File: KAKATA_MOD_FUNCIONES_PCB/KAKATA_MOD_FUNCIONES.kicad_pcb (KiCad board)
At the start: 4 copper layers, 80.3 x 64.3 mm, 61 parts, among them J1 DB128L-5.08-2P-BK-S, J2 Screw_Terminal_01x02, J3 Screw_Terminal_01x02, J4 Screw_Terminal_01x02, J5 DB125-2.54-10P-GN, J6 DB125-2.54-4P-GN, Q1 MMUN2215L, Q2 MMUN2215L, Q3 MMUN2215L, U1 ESP32-S3-WROOM-1(N16R8), U2 PS-TO220, U3 PS-TO220, U4 TYPE-C 16PLT-H10.0

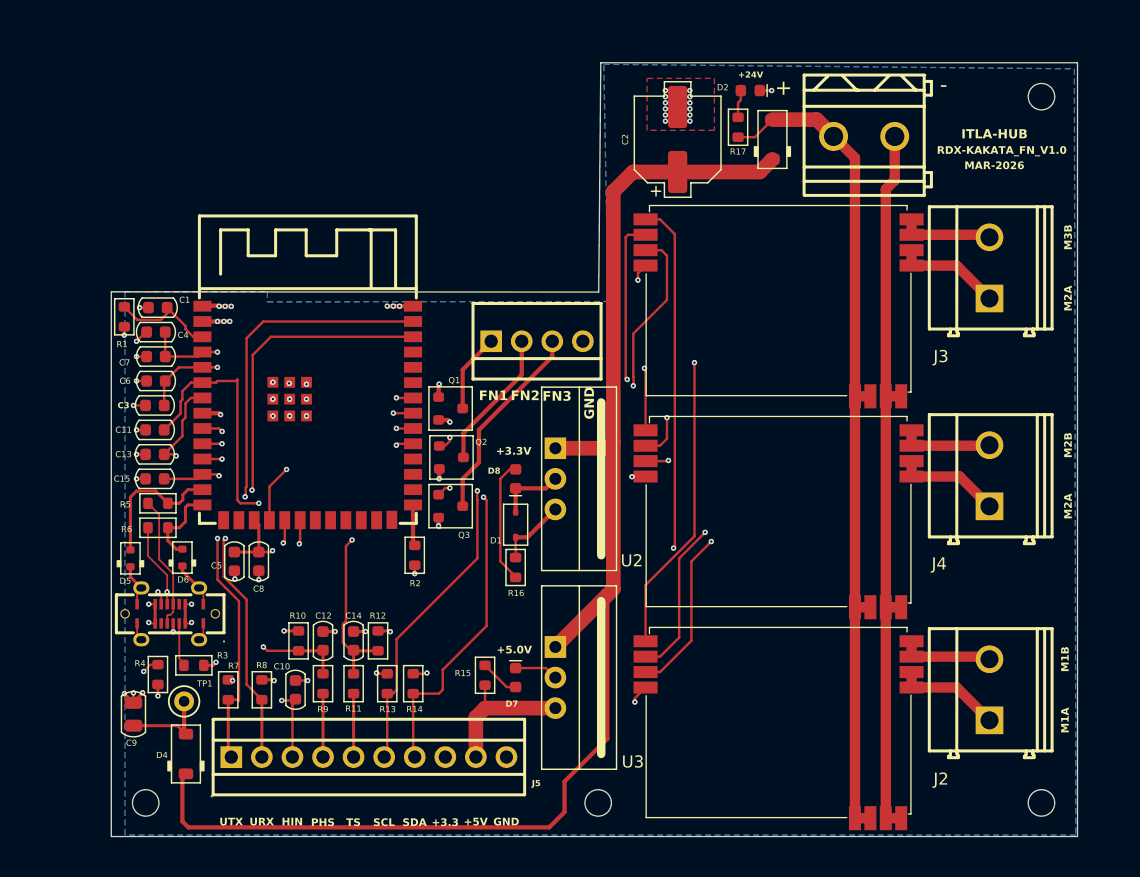
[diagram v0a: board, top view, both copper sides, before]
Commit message: Btn's BOOT y RST agregados. Encendido secuencial implementado
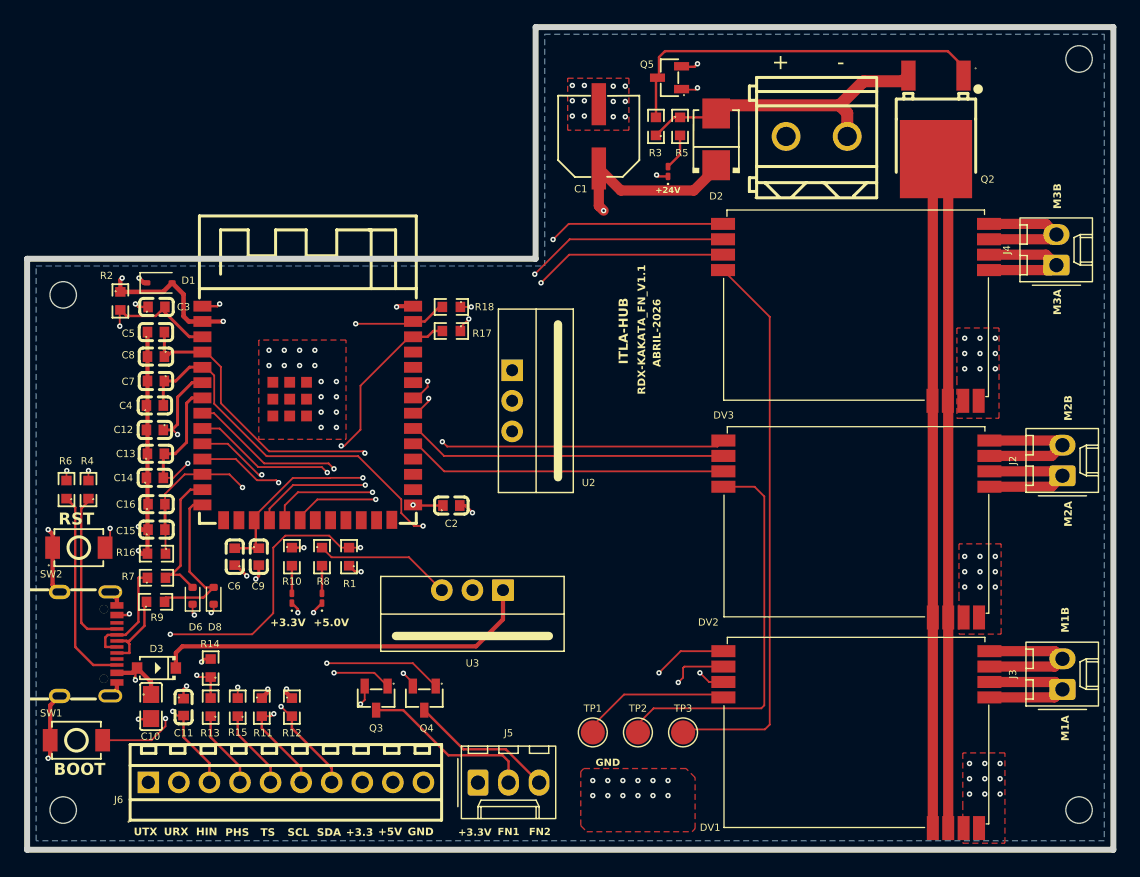
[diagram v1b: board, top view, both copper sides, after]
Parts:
- removed the C1 at (83.1, 63.6)
- removed the D4 at (85.5, 100.6)
- removed Q1: MMUN2215L, PCM_Package_TO_SOT_SMD_AKL:SOT-23
- removed the R15 at (110.3, 94.1)
- removed the R16 at (112.9, 85.2)
- removed U4: TYPE-C 16PLT-H10.0, EasyEDA:TYPE-C-SMD_USB4120-03-C
- added C2: 0.1uF, EasyEDA:C0603, F.Cu at (107.5, 80.0)
- added C3: 1uF, EasyEDA:C0603, F.Cu at (83.0, 63.5)
- added D3: B0540W, EasyEDA:SOD-123_L2.7-W1.6-LS3.7-FD, F.Cu at (83.0, 93.5)
- added Q4: MMUN2215LT1G, EasyEDA:SOT-23-3_L2.9-W1.3-P1.90-LS2.4-BR, F.Cu at (105.3, 96.0)
- added Q5: MMUN2215LT1G, EasyEDA:SOT-23-3_L2.9-W1.3-P1.90-LS2.4-BR, F.Cu at (125.7, 44.5)
- added R10: 220, EasyEDA:R0603, F.Cu at (94.3, 84.3)
- added R3: 10k, EasyEDA:R0603, F.Cu at (124.5, 48.5)
- added R9: 33R, EasyEDA:R0603, F.Cu at (83.0, 88.0)
- added SW1: TS-1088-AR02016, EasyEDA:SW-SMD_L3.9-W3.0-P4.45, F.Cu at (76.4, 99.5)
- added SW2: TS-1088-AR02016, EasyEDA:SW-SMD_L3.9-W3.0-P4.45, F.Cu at (76.6, 83.5)
- added TP2: TestPoint, TestPoint:TestPoint_Pad_D2.0mm, F.Cu at (123.0, 98.9)
- added TP3: TestPoint, TestPoint:TestPoint_Pad_D2.0mm, F.Cu at (126.8, 98.9)
- added USB1: TYPE-C 16PIN 2MD, EasyEDA:USB-C-SMD_TYPE-C-6PIN-2MD-073, F.Cu at (77.4, 91.5)
- C1: renamed from C2; footprint Capacitor_SMD_AKL:CP_Elec_6.3x7.7 -> EasyEDA:CAP-SMD_BD6.3-L6.6-W6.6-LS7.2-FD
- C10: renamed from C9; footprint PCM_Capacitor_SMD_AKL:C_0805_2012Metric -> EasyEDA:C0805
- C11: renamed from C10; footprint PCM_Capacitor_SMD_AKL:C_0603_1608Metric -> EasyEDA:C0603
- C12: renamed from C11; footprint PCM_Capacitor_SMD_AKL:C_0603_1608Metric -> EasyEDA:C0603
- C13: renamed from C12; footprint PCM_Capacitor_SMD_AKL:C_0603_1608Metric -> EasyEDA:C0603
- C14: renamed from C13; footprint PCM_Capacitor_SMD_AKL:C_0603_1608Metric -> EasyEDA:C0603
- C15: renamed from C14; footprint PCM_Capacitor_SMD_AKL:C_0603_1608Metric -> EasyEDA:C0603
- C16: renamed from C15; footprint PCM_Capacitor_SMD_AKL:C_0603_1608Metric -> EasyEDA:C0603
- C4: renamed from C3; footprint PCM_Capacitor_SMD_AKL:C_0603_1608Metric -> EasyEDA:C0603
- C5: renamed from C4; footprint PCM_Capacitor_SMD_AKL:C_0603_1608Metric -> EasyEDA:C0603
- C6: renamed from C5; footprint PCM_Capacitor_SMD_AKL:C_0603_1608Metric -> EasyEDA:C0603
- C7: renamed from C6; footprint PCM_Capacitor_SMD_AKL:C_0603_1608Metric -> EasyEDA:C0603
- C8: renamed from C7; footprint PCM_Capacitor_SMD_AKL:C_0603_1608Metric -> EasyEDA:C0603
- C9: renamed from C8; footprint PCM_Capacitor_SMD_AKL:C_0603_1608Metric -> EasyEDA:C0603
- D1: footprint Diode_SMD_AKL:D_SOD-323_TVS -> Diode_SMD:D_SOD-323
- D2: value B0540LW -> SS24-SMB; footprint Diode_SMD_AKL:D_SOD-123 -> EasyEDA:SMB_L4.3-W3.6-LS5.3-RD
- D4: renamed from D5; value ESD5B5.0S -> Red; footprint PCM_Diode_SMD_AKL:D_SOD-523 -> LED_SMD:LED_0201_0603Metric_Pad0.64x0.40mm_HandSolder
- D5: renamed from D6; value ESD5B5.0S -> Red; footprint PCM_Diode_SMD_AKL:D_SOD-523 -> LED_SMD:LED_0201_0603Metric_Pad0.64x0.40mm_HandSolder
- D6: renamed from D9; value Red -> ESD5B5.0S; footprint SparkFun-LED:LED_0603_1608Metric_Red -> Diode_SMD:D_SOD-523
- D7: footprint SparkFun-LED:LED_0603_1608Metric_Red -> LED_SMD:LED_0201_0603Metric_Pad0.64x0.40mm_HandSolder
- D8: value Red -> ESD5B5.0S; footprint SparkFun-LED:LED_0603_1608Metric_Red -> Diode_SMD:D_SOD-523
- DV1, DV2, DV3: footprint ItlaModules:PHE-3A -> ITLA_Modules:PHE-3A
- J2, J3, J4: value Screw_Terminal_01x02 -> Conn_01x02_Socket; footprint EasyEDA:CONN-TH_2P-P5.08_DIBO_DB128V-5.08 -> Connector_Molex:Molex_KK-254_AE-6410-02A_1x02_P2.54mm_Vertical
- J5: value DB125-2.54-10P-GN -> Conn_01x03_Socket; footprint EasyEDA:CONN-TH_DB125-2.54-10P-GN -> Connector_Molex:Molex_KK-254_AE-6410-03A_1x03_P2.54mm_Vertical
- J6: value DB125-2.54-4P-GN -> DB125-2.54-10P-GN; footprint EasyEDA:CONN-TH_DB125-2.54-4P-GN -> EasyEDA:CONN-TH_DB125-2.54-10P-GN
- Q2: value MMUN2215L -> AOD4185_C400894; footprint PCM_Package_TO_SOT_SMD_AKL:SOT-23 -> EasyEDA:TO-252-3_L6.6-W6.1-P4.57-LS9.9-BR-CW
- Q3: value MMUN2215L -> MMUN2215LT1G; footprint PCM_Package_TO_SOT_SMD_AKL:SOT-23 -> EasyEDA:SOT-23-3_L2.9-W1.3-P1.90-LS2.4-BR
- R1: footprint Resistor_SMD_AKL:R_0603_1608Metric -> EasyEDA:R0603
- R11: renamed from R9; value 2.5K -> 4.7K; footprint PCM_Resistor_SMD_AKL:R_0603_1608Metric -> EasyEDA:R0603
- R12: renamed from R10; value 5K -> 4.7K; footprint PCM_Resistor_SMD_AKL:R_0603_1608Metric -> EasyEDA:R0603
- R13: renamed from R11; value 2.5K -> 5.1K; footprint PCM_Resistor_SMD_AKL:R_0603_1608Metric -> EasyEDA:R0603
- R14: renamed from R12; value 5K -> 5.1K; footprint PCM_Resistor_SMD_AKL:R_0603_1608Metric -> EasyEDA:R0603
- R15: renamed from R7; value 4.5K -> 5.1K; footprint PCM_Resistor_SMD_AKL:R_0603_1608Metric -> EasyEDA:R0603
- R16: renamed from R13; value 2.2K -> 5.1K; footprint PCM_Resistor_SMD_AKL:R_0603_1608Metric -> EasyEDA:R0603
- R17: renamed from R8; value 4.5K -> 4.7K; footprint PCM_Resistor_SMD_AKL:R_0603_1608Metric -> EasyEDA:R0603
- R18: renamed from R14; value 2.2K -> 4.7K; footprint PCM_Resistor_SMD_AKL:R_0603_1608Metric -> EasyEDA:R0603
- R2: footprint PCM_Resistor_SMD_AKL:R_0603_1608Metric -> EasyEDA:R0603
- R4: renamed from R3; footprint PCM_Resistor_SMD_AKL:R_0603_1608Metric -> EasyEDA:R0603
- R5: renamed from R4; value 5.1K -> 4.7K; footprint PCM_Resistor_SMD_AKL:R_0603_1608Metric -> EasyEDA:R0603
- R6: renamed from R5; value 33R -> 5.1K; footprint PCM_Resistor_SMD_AKL:R_0603_1608Metric -> EasyEDA:R0603
- R7: renamed from R6; footprint PCM_Resistor_SMD_AKL:R_0603_1608Metric -> EasyEDA:R0603
- R8: renamed from R17; value 4.7K -> 560; footprint Resistor_SMD_AKL:R_0603_1608Metric -> EasyEDA:R0603
- TP1: value TestPoint_Hole1 -> TestPoint; footprint 4ms_TestPoint:TestPoint_WireHole -> TestPoint:TestPoint_Pad_D2.0mm
- moved R5 62.9 mm to (126.5, 48.5)
- moved D6 62.5 mm to (86.0, 87.5), turned to 90 degrees
- moved H4 61.3 mm to (75.3, 62.5)
- moved D4 55.0 mm to (125.5, 52.3)
- moved R8 49.7 mm to (96.8, 84.3), turned to -90 degrees
- moved Q2 49.2 mm to (147.8, 47.8), turned to 90 degrees
- moved J6 42.2 mm to (93.8, 103.0)
- moved D1 35.8 mm to (83.3, 61.5), turned to 0 degrees
- moved J3 35.5 mm to (158.3, 95.3)
- moved TP1 34.1 mm to (119.3, 98.9)
- moved R17 33.7 mm to (107.5, 65.5), turned to 180 degrees
- moved R2 32.3 mm to (80.0, 63.0), turned to -90 degrees
- moved R18 31.5 mm to (107.5, 63.5), turned to 180 degrees
- moved R1 27.3 mm to (99.0, 84.3)
- moved D8 26.9 mm to (87.8, 87.5)
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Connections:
- D4 pad 2: /USB_D- -> Net-(D4-A)
- D5 pad 2: /USB_D+ -> Net-(D5-A)
- D6 pad 2: Net-(D9-A) -> /USB_D-
- D8 pad 2: Net-(D8-A) -> /USB_D+
- DV1 pad 12: +24V -> V_DRIVER
- DV1 pad 4: +3.3V -> Net-(DV1-Vref)
- DV1 pad 8: +24V -> V_DRIVER
- DV2 pad 12: +24V -> V_DRIVER
- DV2 pad 4: +3.3V -> Net-(DV2-Vref)
- DV2 pad 8: +24V -> V_DRIVER
- DV3 pad 12: +24V -> V_DRIVER
- DV3 pad 4: +3.3V -> Net-(DV3-Vref)
- DV3 pad 8: +24V -> V_DRIVER
- J2 pad 1: /MOTOR1_A -> /MOTOR2_A
- J2 pad 2: /MOTOR1_B -> /MOTOR2_B
- J3 pad 1: /MOTOR3_A -> /MOTOR1_A
- J3 pad 2: /MOTOR3_B -> /MOTOR1_B
- J4 pad 1: /MOTOR2_A -> /MOTOR3_A
- J4 pad 2: /MOTOR2_B -> /MOTOR3_B
- J5 pad 1: /UART_TXD_CO2 -> +3.3V
- J5 pad 2: /UART_RXD_CO2 -> Net-(J5-Pin_2)
- J5 pad 3: /H_IN -> Net-(J5-Pin_3)
- J6 pad 1: /FN1 -> /UART_TXD_CO2
- J6 pad 2: /FN2 -> /UART_RXD_CO2
- J6 pad 3: /FN3 -> /H_IN
- J6 pad 4: GND -> /CON_PH_SENSE
- Q2 pad 1: /ACT_2 -> Net-(Q2-G)
- Q2 pad 2: GND -> V_DRIVER
- Q2 pad 3: /FN2 -> +24V
- Q3 pad 1: /ACT_3 -> /ACT_1
- Q3 pad 3: /FN3 -> Net-(J5-Pin_2)
- R1 pad 2: /EN -> /BOOT
- R11 pad 1: /CON_PH_SENSE -> +3.3V
- R11 pad 2: /PH_SENSE -> /I2C_SCL
- R12 pad 1: /PH_SENSE -> +3.3V
- R12 pad 2: GND -> /I2C_SDA
- R13 pad 1: /CON_T_SENSE -> /CON_PH_SENSE
- R13 pad 2: /T_SENSE -> /PH_SENSE
- R14 pad 1: /T_SENSE -> /PH_SENSE
- R15 pad 1: +3.3V -> /CON_T_SENSE
- R15 pad 2: /UART_TXD_CO2 -> /T_SENSE
- R16 pad 1: +3.3V -> /T_SENSE
- R16 pad 2: /I2C_SCL -> GND
- R17 pad 2: /UART_RXD_CO2 -> /UART_TXD_CO2
- R18 pad 2: /I2C_SDA -> /UART_RXD_CO2
- R2 pad 2: /BOOT -> /CHIP_PU
- R5 pad 1: Net-(U4-CC2) -> +24V
- R5 pad 2: GND -> Net-(D4-A)
- R6 pad 2: /USB_D- -> GND
- R7 pad 2: /USB_D+ -> /USB_D-
- R8 pad 1: +24V -> +5V
- R8 pad 2: Net-(D9-A) -> Net-(D5-A)
- TP1 pad 1: VBUS -> Net-(DV1-Vref)
- U1 pad 3: /EN -> /CHIP_PU
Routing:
- net V_DRIVER: track 0.00 -> 111.7 mm
- net GND: track 107.6 -> 56.8 mm, vias 51 -> 91
- net /ACT_3: track 20.3 -> 69.6 mm
- net Net-(DV3-Vref): track 0.00 -> 46.2 mm
- net +24V: track 70.3 -> 25.9 mm
- net /BOOT: track 3.42 -> 46.1 mm, vias 0 -> 4
- net Net-(DV2-Vref): track 0.00 -> 32.4 mm
- net Net-(Q2-G): track 0.00 -> 31.9 mm
- net /CHIP_PU: track 0.00 -> 29.1 mm, vias 0 -> 2
- net VCC: track 115.2 -> 91.6 mm, vias 0 -> 1
- net +5V: track 12.1 -> 29.1 mm
- net /FN3: track 16.8 -> 0.00 mm
- net /I2C_SDA: track 50.6 -> 33.9 mm
- net /I2C_SCL: track 50.1 -> 34.2 mm
- net /ACT_2: track 22.6 -> 37.6 mm
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- removed copper zone on In2.Cu, net VBUS
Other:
- board size 80.3 x 64.3 mm -> 90.2 x 68.3 mm
- board text added: "ABRIL-2026"
- board text added: "BOOT"
- board text added: "M3A"
- board text added: "RDX-KAKATA_FN_V1.1"
- board text added: "RST"
- board text removed: "FN3"
- board text removed: "MAR-2026"
- board text removed: "RDX-KAKATA_FN_V1.0"
